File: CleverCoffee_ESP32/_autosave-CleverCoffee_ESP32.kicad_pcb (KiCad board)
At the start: 2 copper layers, 95 x 65 mm, 37 parts

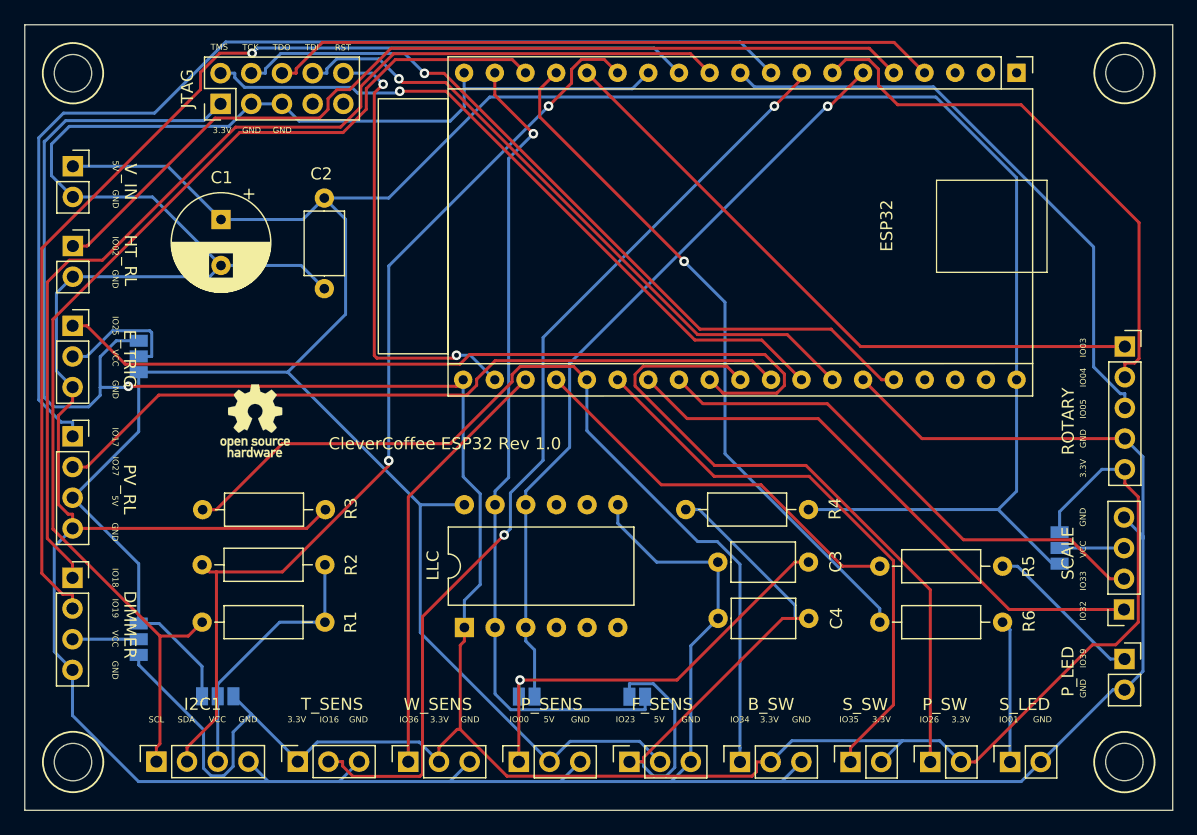
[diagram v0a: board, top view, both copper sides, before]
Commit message: Consolidate designs into one PCB
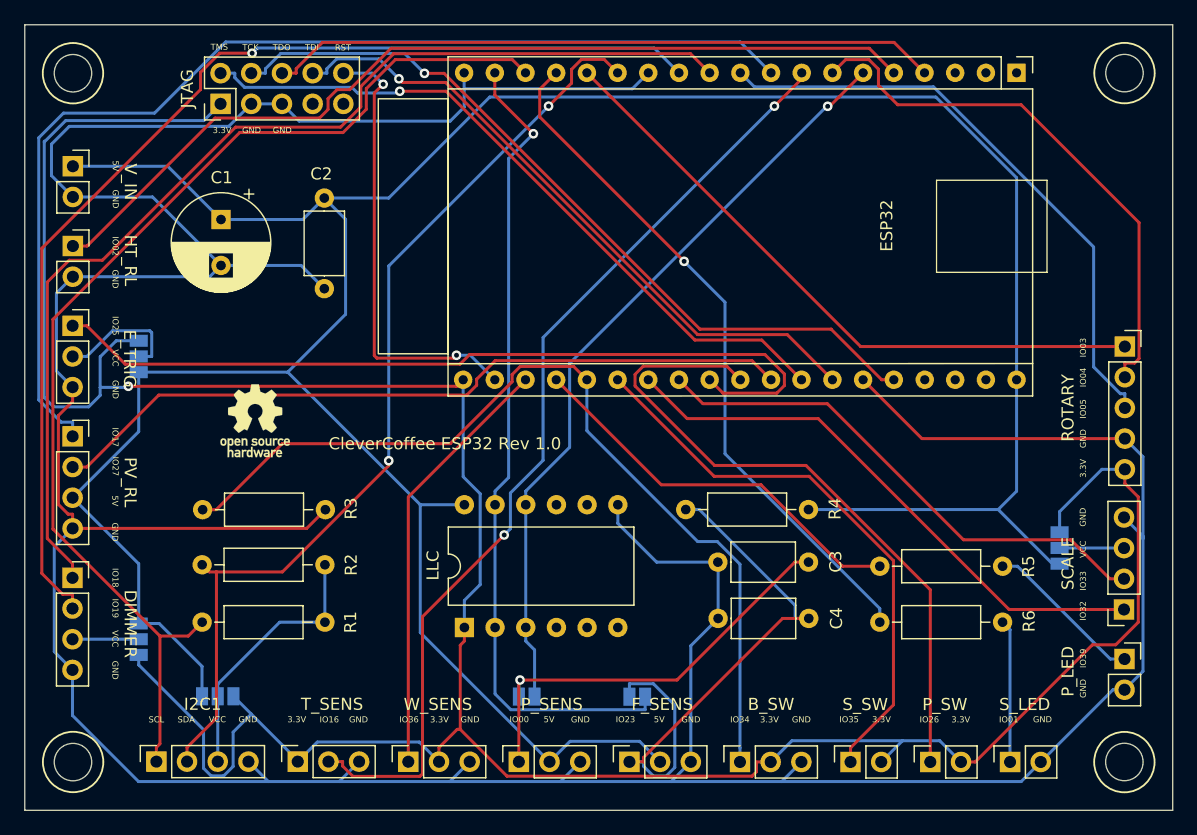
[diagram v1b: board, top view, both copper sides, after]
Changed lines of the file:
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@@
     (property "Sheetname" "")
     (attr through_hole)
-    (fp_text reference "PV_RL" (at 4.71 4.39 270 unlocked) (layer "F.SilkS")
+    (fp_text reference "PV_RL" (at 4.77 3.8 270 unlocked) (layer "F.SilkS")
       (effects (font (size 1 1) (thickness 0.15)))
     )
@@
     (property "Sheetname" "")
     (attr through_hole)
-    (fp_text reference "SCALE" (at 4.64 4.65 90) (layer "F.SilkS")
+    (fp_text reference "SCALE" (at 4.64 3.81 90) (layer "F.SilkS")
       (effects (font (size 1 1) (thickness 0.15)))
     )
@@
     (property "Sheetname" "")
     (attr through_hole)
-    (fp_text reference "ROTARY" (at -4.69 6.19 90) (layer "F.SilkS")
+    (fp_text reference "ROTARY" (at -4.71 5.08 90) (layer "F.SilkS")
       (effects (font (size 1 1) (thickness 0.15)))
     )
@@
     (property "Sheetname" "")
     (attr through_hole)
-    (fp_text reference "DIMMER" (at 4.75 3.88 270 unlocked) (layer "F.SilkS")
-      (effects (font (size 1 1) (thickness 0.15)))
-    )
+    (fp_text reference "DIMMER" (at 4.78 3.81 270 unlocked) (layer "F.SilkS")
+      (effects (font (size 1 1) (thickness 0.15)))
+    )
